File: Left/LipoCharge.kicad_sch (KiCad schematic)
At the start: 4 parts, among them U33 TP4054

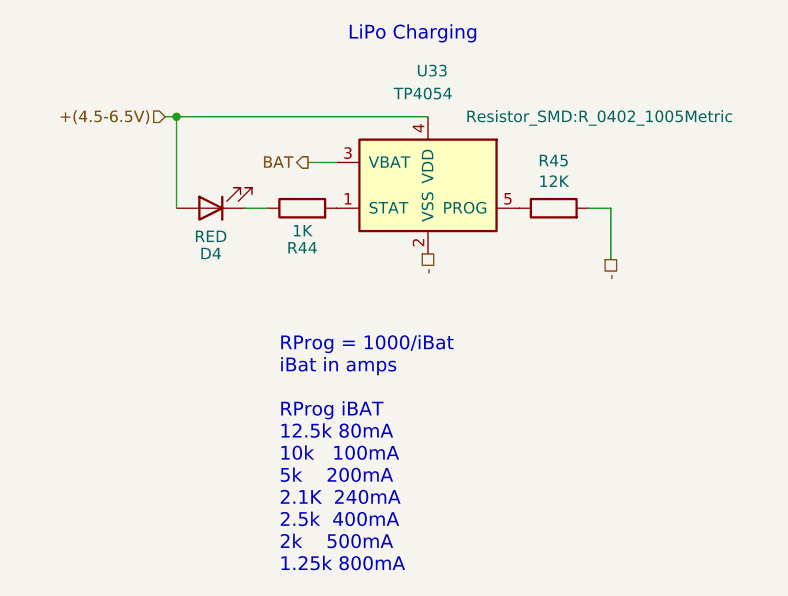
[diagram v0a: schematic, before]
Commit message: upgraded files to kicad7
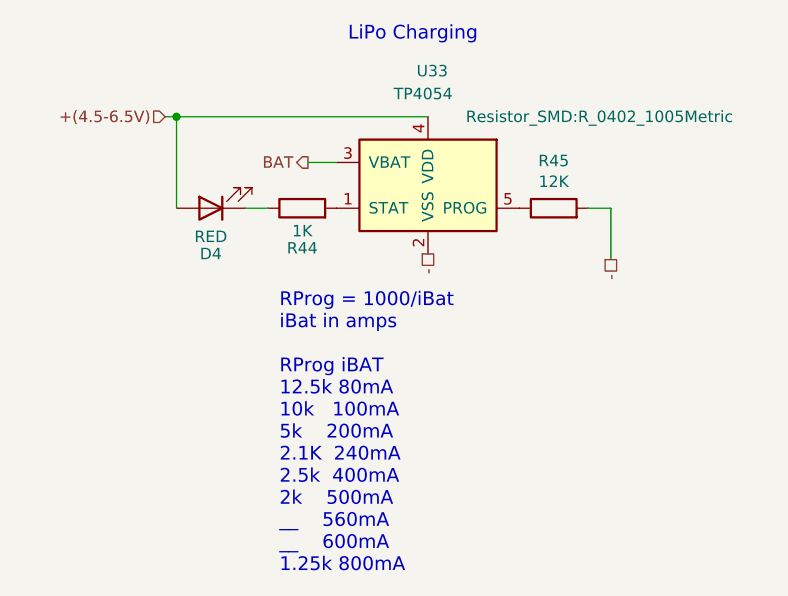
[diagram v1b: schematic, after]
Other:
- note added: "RProg = 1000/iBat iBat in amps RProg iBAT 12.5k 80mA 10k 100mA 5k 200mA 2.1K 240mA 2.5k 400mA 2k 500mA __ 560mA __ 600mA 1.25k 800mA"
- note removed: "RProg = 1000/iBat iBat in amps RProg iBAT 12.5k 80mA 10k 100mA 5k 200mA 2.1K 240mA 2.5k 400mA 2k 500mA 1.25k 800mA"
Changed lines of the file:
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@@
-(kicad_sch (version 20211123) (generator eeschema)
+(kicad_sch (version 20230121) (generator eeschema)
   (paper "A5")
   (junction (at 76.2 48.26) (diameter 0) (color 0 0 0 0)
   )
   (wire (pts (xy 83.82 58.42) (xy 86.36 58.42))
-    (stroke (width 0) (type default) (color 0 0 0 0))
+    (stroke (width 0) (type default))
   )
   (wire (pts (xy 76.2 58.42) (xy 76.2 48.26))
-    (stroke (width 0) (type default) (color 0 0 0 0))
+    (stroke (width 0) (type default))
   )
   (wire (pts (xy 124.46 58.42) (xy 124.46 64.135))
-    (stroke (width 0) (type default) (color 0 0 0 0))
+    (stroke (width 0) (type default))
   )
   (wire (pts (xy 76.2 48.26) (xy 104.14 48.26))
-    (stroke (width 0) (type default) (color 0 0 0 0))
+    (stroke (width 0) (type default))
   )
   (wire (pts (xy 74.93 48.26) (xy 76.2 48.26))
-    (stroke (width 0) (type default) (color 0 0 0 0))
+    (stroke (width 0) (type default))
   )
   (wire (pts (xy 90.805 53.34) (xy 93.98 53.34))
-    (stroke (width 0) (type default) (color 0 0 0 0))
+    (stroke (width 0) (type default))
   )
   (wire (pts (xy 121.92 58.42) (xy 124.46 58.42))
-    (stroke (width 0) (type default) (color 0 0 0 0))
+    (stroke (width 0) (type default))
   )
-  (text "RProg = 1000/iBat\niBat in amps\n\nRProg iBAT\n12.5k 80mA\n10k   100mA\n5k    200mA\n2.1K  240mA\n2.5k  400mA\n2k    500mA\n1.25k 800mA"
+  (text "RProg = 1000/iBat\niBat in amps\n\nRProg iBAT\n12.5k 80mA\n10k   100mA\n5k    200mA\n2.1K  240mA\n2.5k  400mA\n2k    500mA\n__    560mA\n__    600mA\n1.25k 800mA"
     (at 87.63 99.06 0)
     (effects (font (size 1.524 1.524)) (justify left bottom))
@@
     (effects (font (size 1.524 1.524)) (justify left bottom))
   )
-  (hierarchical_label "-" (shape passive) (at 104.14 63.5 270)
+  (hierarchical_label "-" (shape passive) (at 104.14 63.5 270) (fields_autoplaced)
     (effects (font (size 1.27 1.27)) (justify right))
   )
-  (hierarchical_label "BAT" (shape output) (at 90.805 53.34 180)
+  (hierarchical_label "BAT" (shape output) (at 90.805 53.34 180) (fields_autoplaced)
     (effects (font (size 1.27 1.27)) (justify right))
   )
-  (hierarchical_label "+(4.5-6.5V)" (shape input) (at 74.93 48.26 180)
+  (hierarchical_label "+(4.5-6.5V)" (shape input) (at 74.93 48.26 180) (fields_autoplaced)
     (effects (font (size 1.27 1.27)) (justify right))
   )
-  (hierarchical_label "-" (shape passive) (at 124.46 64.135 270)
+  (hierarchical_label "-" (shape passive) (at 124.46 64.135 270) (fields_autoplaced)
     (effects (font (size 1.27 1.27)) (justify right))
   )
   (symbol (lib_id "Battery_Management:MCP73832-2-OT") (at 104.14 55.88 0) (mirror y) (unit 1)
-    (in_bom yes) (on_board yes)
-    (property "Reference" "U33" (id 0) (at 102.87 43.18 0)
+    (in_bom yes) (on_board yes) (dnp no)
+    (property "Reference" "U33" (at 102.87 43.18 0)
       (effects (font (size 1.27 1.27)) (justify right))
     )
-    (property "Value" "TP4054" (id 1) (at 100.33 45.72 0)
+    (property "Value" "TP4054" (at 100.33 45.72 0)
       (effects (font (size 1.27 1.27)) (justify right))
     )
-    (property "Footprint" "Package_TO_SOT_SMD:SOT-23-5" (id 2) (at 102.87 62.23 0)
+    (property "Footprint" "Package_TO_SOT_SMD:SOT-23-5" (at 102.87 62.23 0)
       (effects (font (size 1.27 1.27) italic) (justify left) hide)
     )
-    (property "Datasheet" "http://ww1.microchip.com/downloads/en/DeviceDoc/20001984g.pdf" (id 3) (at 107.95 57.15 0)
+    (property "Datasheet" "http://ww1.microchip.com/downloads/en/DeviceDoc/20001984g.pdf" (at 107.95 57.15 0)
       (effects (font (size 1.27 1.27)) hide)
     )
@@
     (pin "4")
     (pin "5")
+    (instances
+      (project "Left"
+        (path "/94899d91-c8b6-48a0-9eee-db2609092a2a/9bf2ab01-30ce-4ac1-8d76-82f9ba33ea19"
+          (reference "U33") (unit 1)
+        )
+      )
+    )
   )
   (symbol (lib_id "nrfmicro-rescue:R") (at 90.17 58.42 90) (unit 1)
-    (in_bom yes) (on_board yes)
-    (property "Reference" "R44" (id 0) (at 90.17 62.865 90))
-    (property "Value" "1K" (id 1) (at 90.17 60.96 90))
-    (property "Footprint" "Resistor_SMD:R_0402_1005Metric" (id 2) (at 90.17 60.198 90)
+    (in_bom yes) (on_board yes) (dnp no)
+    (property "Reference" "R44" (at 90.17 62.865 90)
+      (effects (font (size 1.27 1.27)))
+    )
+    (property "Value" "1K" (at 90.17 60.96 90)
+      (effects (font (size 1.27 1.27)))
+    )
+    (property "Footprint" "Resistor_SMD:R_0402_1005Metric" (at 90.17 60.198 90)
       (effects (font (size 1.27 1.27)) hide)
     )
-    (property "Datasheet" "" (id 3) (at 90.17 58.42 0)
+    (property "Datasheet" "" (at 90.17 58.42 0)
       (effects (font (size 1.27 1.27)) hide)
     )
     (pin "1")
     (pin "2")
+    (instances
+      (project "Left"
+        (path "/94899d91-c8b6-48a0-9eee-db2609092a2a/9bf2ab01-30ce-4ac1-8d76-82f9ba33ea19"
+          (reference "R44") (unit 1)
+        )
+      )
+    )
   )
   (symbol (lib_id "nrfmicro-rescue:R") (at 118.11 58.42 90) (unit 1)
-    (in_bom yes) (on_board yes)
-    (property "Reference" "R45" (id 0) (at 118.11 53.1622 90))
-    (property "Value" "12K" (id 1) (at 118.11 55.4736 90))
-    (property "Footprint" "Resistor_SMD:R_0402_1005Metric" (id 2) (at 123.19 48.26 90))
-    (property "Datasheet" "" (id 3) (at 118.11 58.42 0)
+    (in_bom yes) (on_board yes) (dnp no)
+    (property "Reference" "R45" (at 118.11 53.1622 90)
+      (effects (font (size 1.27 1.27)))
+    )
+    (property "Value" "12K" (at 118.11 55.4736 90)
+      (effects (font (size 1.27 1.27)))
+    )
+    (property "Footprint" "Resistor_SMD:R_0402_1005Metric" (at 123.19 48.26 90)
+      (effects (font (size 1.27 1.27)))
+    )
+    (property "Datasheet" "" (at 118.11 58.42 0)
       (effects (font (size 1.27 1.27)) hide)
     )
     (pin "1")
     (pin "2")
+    (instances
+      (project "Left"
+        (path "/94899d91-c8b6-48a0-9eee-db2609092a2a/9bf2ab01-30ce-4ac1-8d76-82f9ba33ea19"
+          (reference "R45") (unit 1)
+        )
+      )
+    )
   )
   (symbol (lib_id "Device:LED") (at 80.01 58.42 180) (unit 1)
-    (in_bom yes) (on_board yes)
-    (property "Reference" "D4" (id 0) (at 80.01 63.5 0))
-    (property "Value" "RED" (id 1) (at 80.01 61.595 0))
-    (property "Footprint" "LED_SMD:LED_0402_1005Metric" (id 2) (at 80.01 58.42 0)
+    (in_bom yes) (on_board yes) (dnp no)
+    (property "Reference" "D4" (at 80.01 63.5 0)
+      (effects (font (size 1.27 1.27)))
+    )
+    (property "Value" "RED" (at 80.01 61.595 0)
+      (effects (font (size 1.27 1.27)))
+    )
+    (property "Footprint" "LED_SMD:LED_0402_1005Metric" (at 80.01 58.42 0)
       (effects (font (size 1.27 1.27)) hide)
     )
-    (property "Datasheet" "~" (id 3) (at 80.01 58.42 0)
+    (property "Datasheet" "~" (at 80.01 58.42 0)
       (effects (font (size 1.27 1.27)) hide)
     )
     (pin "1")
     (pin "2")
+    (instances
+      (project "Left"
+        (path "/94899d91-c8b6-48a0-9eee-db2609092a2a/9bf2ab01-30ce-4ac1-8d76-82f9ba33ea19"
+          (reference "D4") (unit 1)
+        )
+      )
+    )
   )
 )
